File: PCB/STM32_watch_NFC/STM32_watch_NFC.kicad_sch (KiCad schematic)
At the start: 60 parts, among them J1 Conn_01x06_Socket, Q1 2N7000, SW1 SW_DPST_x2, SW2 SW_DPST_x2, SW3 SW_DPST_x2, U1 STM32L031G6Ux, Y2 32.768kHz

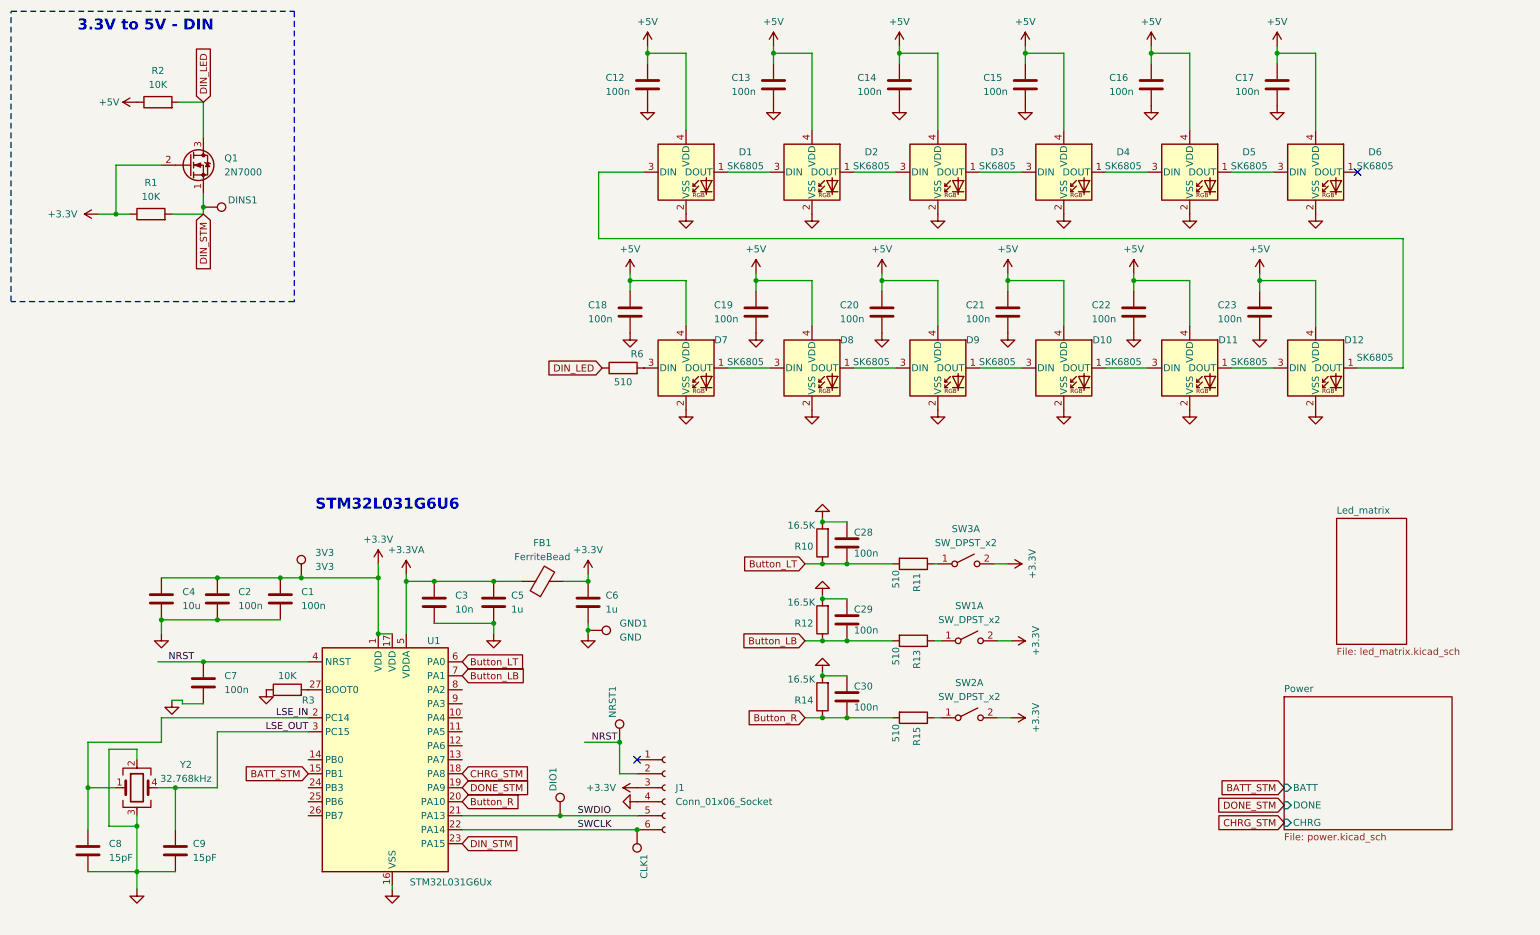
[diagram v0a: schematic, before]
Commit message: Kicad - new Routing 1
Led matrix sheet added
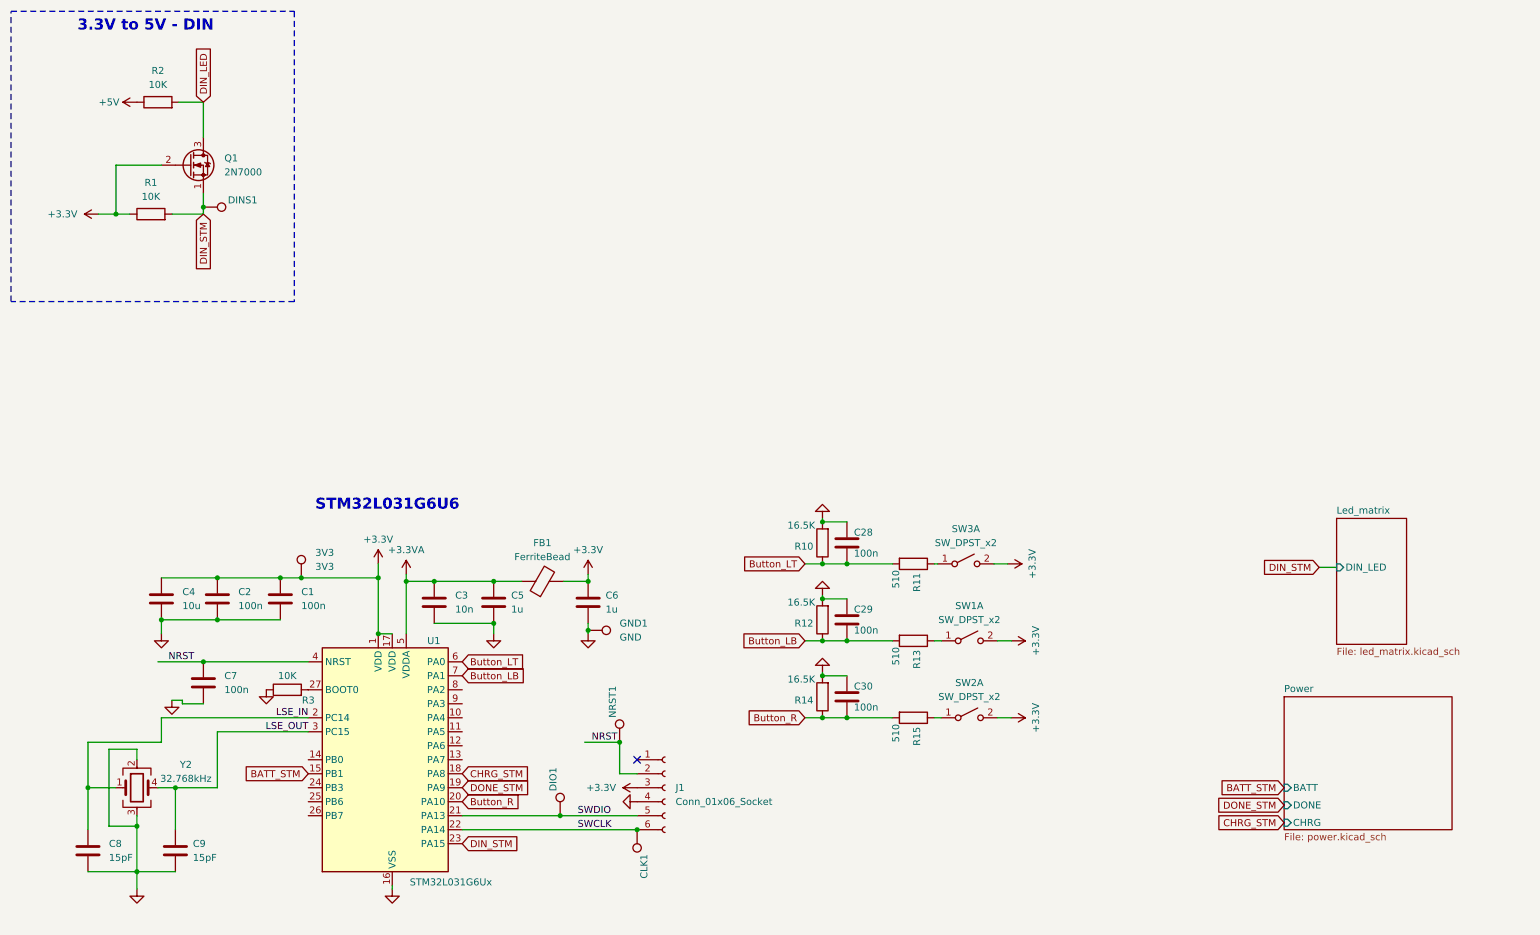
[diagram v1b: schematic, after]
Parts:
- removed C12, C13, C14, C15, C16, C17, C18, C19, C20, C21, C22, C23: 100n, Capacitor_SMD:C_0201_0603Metric, symbol Device:C
- removed D1, D10, D11, D12, D2, D3, D4, D5, D6, D7, D8, D9: SK6805, LED_SMD:LED_SK6812_EC15_1.5x1.5mm, symbol LED:SK6805
- removed R6: 510, Resistor_SMD:R_0402_1005Metric, symbol Device:R
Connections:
- no-connect marks 2 -> 1
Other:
- sheet Led_matrix ports: added DIN_LED; removed none

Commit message: Kicad - new Routing 2
4 7-segment RGB displays for time - pretty crazy I would say
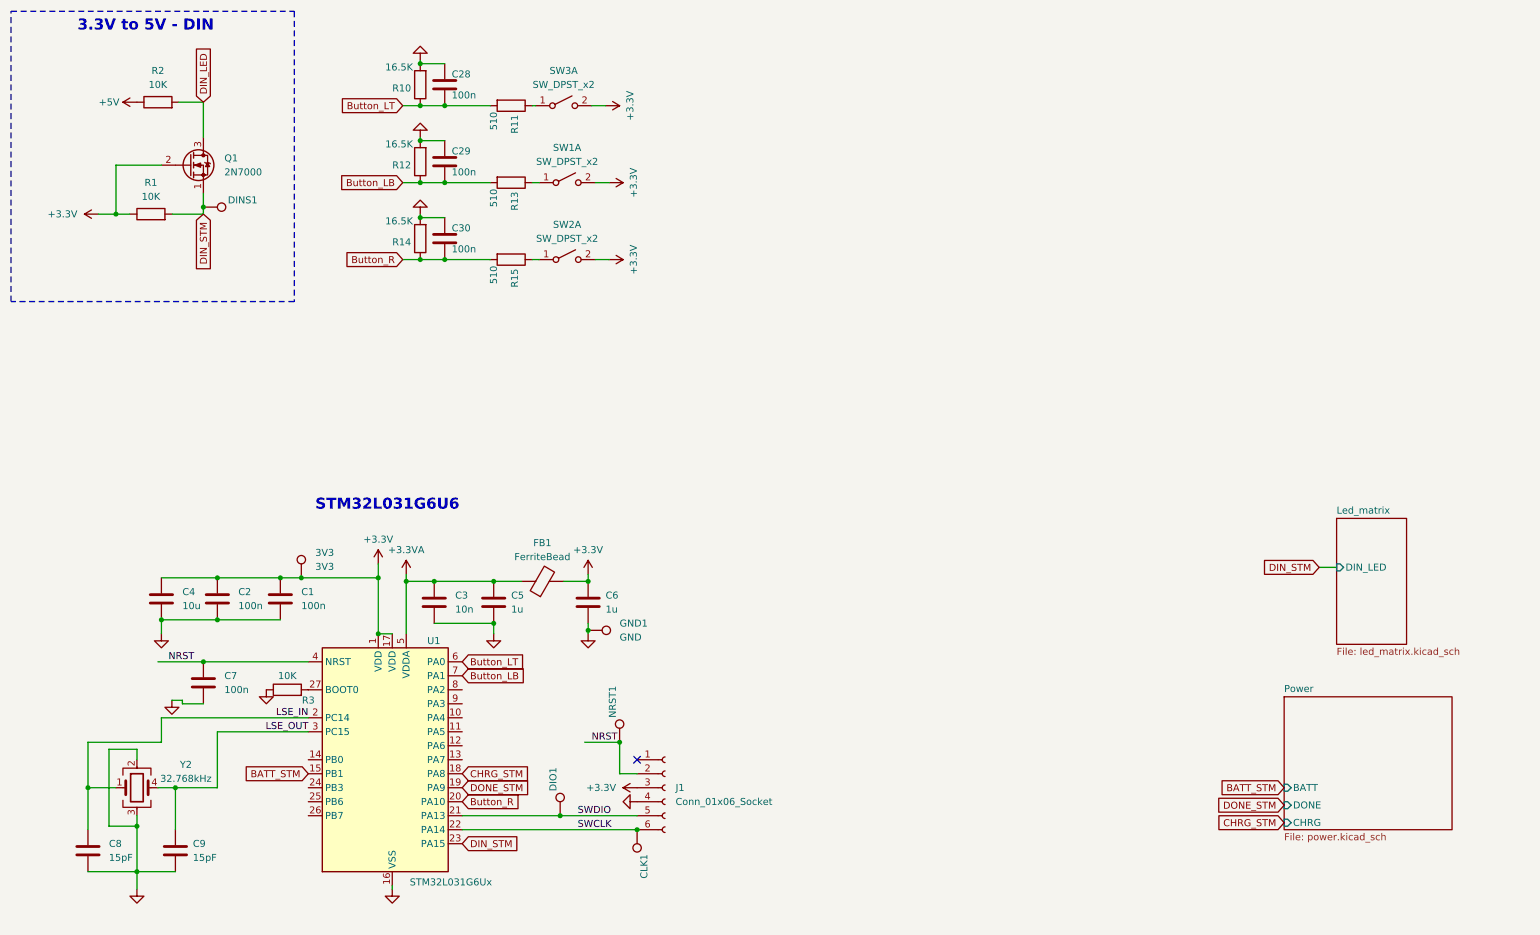
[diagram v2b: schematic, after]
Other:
- moved on the sheet: C28, C29, C30, R10, R11, R12, R13, R14, R15, SW1A, SW2A, SW3A

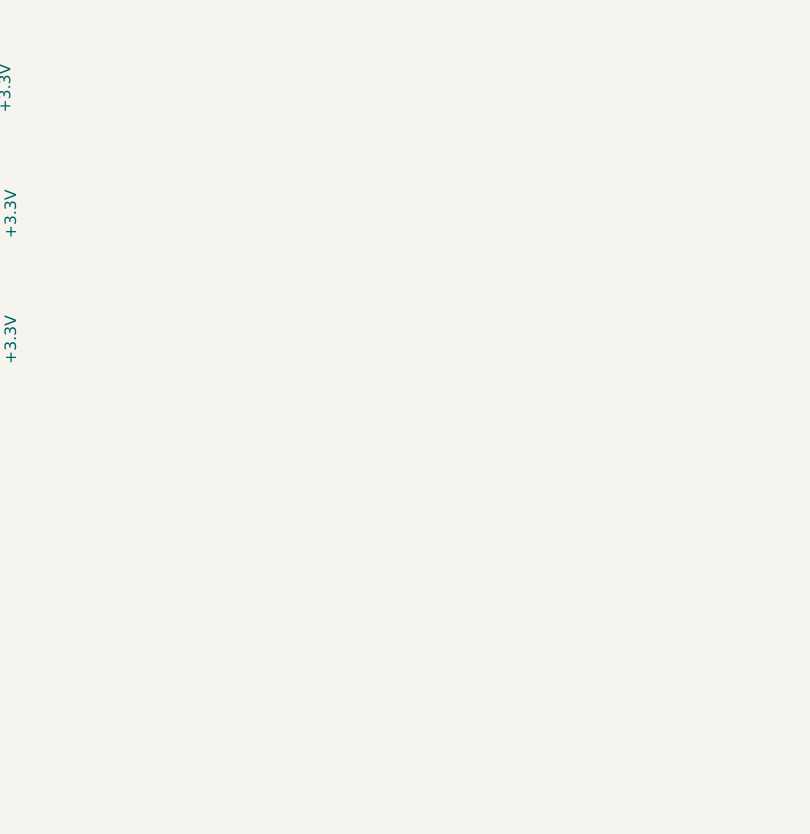
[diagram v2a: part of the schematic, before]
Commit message: Kicad - new Routing 3
TM1637 7-segment driver
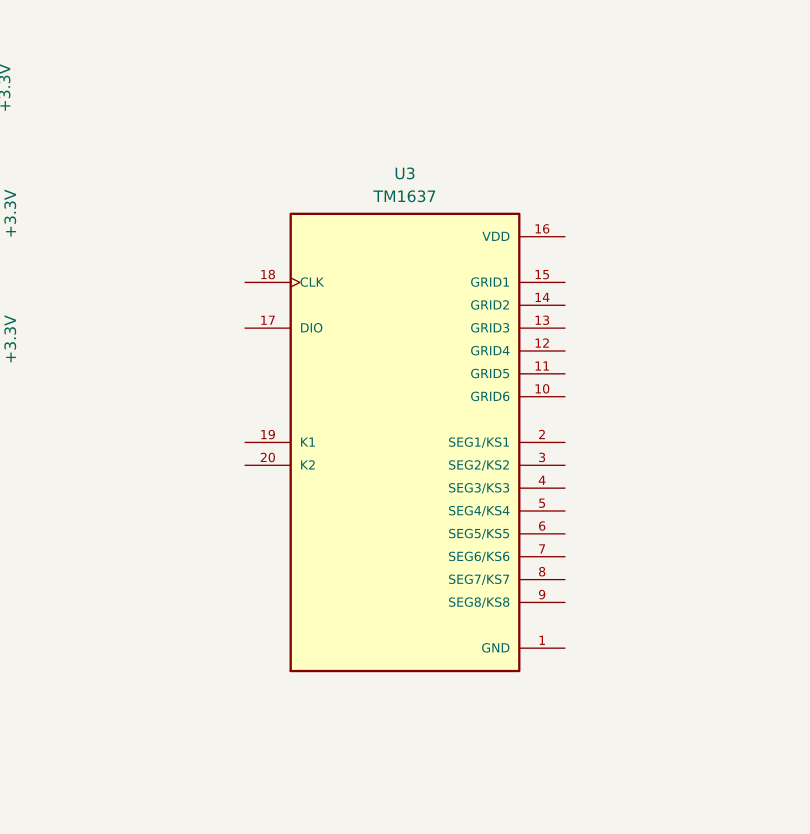
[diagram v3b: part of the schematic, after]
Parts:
- added U3: TM1637, Package_SO:SOP-20_7.5x12.8mm_P1.27mm, symbol TM1637:TM1637
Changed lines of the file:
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@@
 	(label "LSE_IN"
 		(at 66.04 140.335 180)
-		(fields_autoplaced yes)
 		(effects
 			(font
@@
 	(label "SWCLK"
 		(at 114.935 160.655 0)
-		(fields_autoplaced yes)
 		(effects
 			(font
@@
 	(label "NRST"
 		(at 40.64 130.175 0)
-		(fields_autoplaced yes)
 		(effects
 			(font
@@
 	(label "LSE_OUT"
 		(at 66.04 142.875 180)
-		(fields_autoplaced yes)
 		(effects
 			(font
@@
 	(label "NRST"
 		(at 117.475 144.78 0)
-		(fields_autoplaced yes)
 		(effects
 			(font
@@
 	(label "SWDIO"
 		(at 114.935 158.115 0)
-		(fields_autoplaced yes)
 		(effects
 			(font
@@
 					(unit 1)
 				)
+			)
+		)
+	)
+	(symbol
+		(lib_id "TM1637:TM1637")
+		(at 168.91 68.58 0)
+		(unit 1)
+		(exclude_from_sim no)
+		(in_bom yes)
+		(on_board yes)
+		(dnp no)
+		(fields_autoplaced yes)
+		(property "Reference" "U3"
+			(at 168.91 38.735 0)
+			(effects
+				(font
+					(size 1.27 1.27)
+				)
+			)
+		)
+		(property "Value" "TM1637"
+			(at 168.91 41.275 0)
+			(effects
+				(font
+					(size 1.27 1.27)
+				)
+			)
+		)
+		(property "Footprint" "Package_SO:SOP-20_7.5x12.8mm_P1.27mm"
+			(at 168.91 68.58 0)
+			(effects
+				(font
+					(size 1.27 1.27)
+				)
+				(justify bottom)
+				(hide yes)
+			)
+		)
+		(property "Datasheet" ""
+			(at 168.91 68.58 0)
+			(effects
+				(font
+					(size 1.27 1.27)
+				)
+				(hide yes)
+			)
+		)
+		(property "Description" ""
+			(at 168.91 68.58 0)
+			(effects
+				(font
+					(size 1.27 1.27)
+				)
+				(hide yes)
+			)
+		)
+		(property "MF" "Titan Micro Electronics"
+			(at 168.91 68.58 0)
+			(effects
+				(font
+					(size 1.27 1.27)
+				)
+				(justify bottom)
+				(hide yes)
+			)
+		)
+		(property "MAXIMUM_PACKAGE_HEIGHT" "4.31 mm"
+			(at 168.91 68.58 0)
+			(effects
+				(font
+					(size 1.27 1.27)
+				)
+				(justify bottom)
+				(hide yes)
+			)
+		)
+		(property "Package" "None"
+			(at 168.91 68.58 0)
+			(effects
+				(font
+					(size 1.27 1.27)
+				)
+				(justify bottom)
+				(hide yes)
+			)
+		)
+		(property "Price" "None"
+			(at 168.91 68.58 0)
+			(effects
+				(font
+					(size 1.27 1.27)
+				)
+				(justify bottom)
+				(hide yes)
+			)
+		)
+		(property "Check_prices" "https://www.snapeda.com/parts/TM1637/Titan+Micro+Electronics/view-part/?ref=eda"
+			(at 168.91 68.58 0)
+			(effects
+				(font
+					(size 1.27 1.27)
+				)
+				(justify bottom)
+				(hide yes)
+			)
+		)
+		(property "STANDARD" "IPC 7351B"
+			(at 168.91 68.58 0)
+			(effects
+				(font
+					(size 1.27 1.27)
+				)
+				(justify bottom)
+				(hide yes)
+			)
+		)
+		(property "PARTREV" "v2.5"
+			(at 168.91 68.58 0)
+			(effects
+				(font
+					(size 1.27 1.27)
+				)
+				(justify bottom)
+				(hide yes)
+			)
+		)
+		(property "SnapEDA_Link" "https://www.snapeda.com/parts/TM1637/Titan+Micro+Electronics/view-part/?ref=snap"
+			(at 168.91 68.58 0)
+			(effects
+				(font
+					(size 1.27 1.27)
+				)
+				(justify bottom)
+				(hide yes)
+			)
+		)
+		(property "MP" "TM1637"
+			(at 168.91 68.58 0)
+			(effects
+				(font
+					(size 1.27 1.27)
+				)
+				(justify bottom)
+				(hide yes)
+			)
+		)
+		(property "Description_1" "\n                        \n                            LED Drive Control Special Circuit\n                        \n"
+			(at 168.91 68.58 0)
+			(effects
+				(font
+					(size 1.27 1.27)
+				)
+				(justify bottom)
+				(hide yes)
+			)
+		)
+		(property "Availability" "Not in stock"
+			(at 168.91 68.58 0)
+			(effects
+				(font
+					(size 1.27 1.27)
+				)
+				(justify bottom)
+				(hide yes)
+			)
+		)
+		(property "MANUFACTURER" "Titan Micro Electronics"
+			(at 168.91 68.58 0)
+			(effects
+				(font
+					(size 1.27 1.27)
+				)
+				(justify bottom)
+				(hide yes)
+			)
+		)
+		(pin "3"
+		)
+		(pin "4"
+		)
+		(pin "8"
+		)
+		(pin "16"
+		)
+		(pin "5"
+		)
+		(pin "20"
+		)
+		(pin "2"
+		)
+		(pin "11"
+		)
+		(pin "9"
+		)
+		(pin "13"
+		)
+		(pin "6"
+		)
+		(pin "14"
+		)
+		(pin "10"
+		)
+		(pin "12"
+		)
+		(pin "15"
+		)
+		(pin "19"
+		)
+		(pin "18"
+		)
+		(pin "7"
+		)
+		(pin "17"
+		)
+		(pin "1"
+		)
+		(instances
+			(project ""
+				(path "/e445874f-c7a3-43dd-b930-6bce1d4fa2ef"
+					(reference "U3")
+					(unit 1)
+				)
